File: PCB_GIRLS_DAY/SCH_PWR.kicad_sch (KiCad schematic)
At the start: 8 parts, among them J3 Conn_01x03_Pin, U3 AP2112K-3.3, U4 AMS1117-5.0

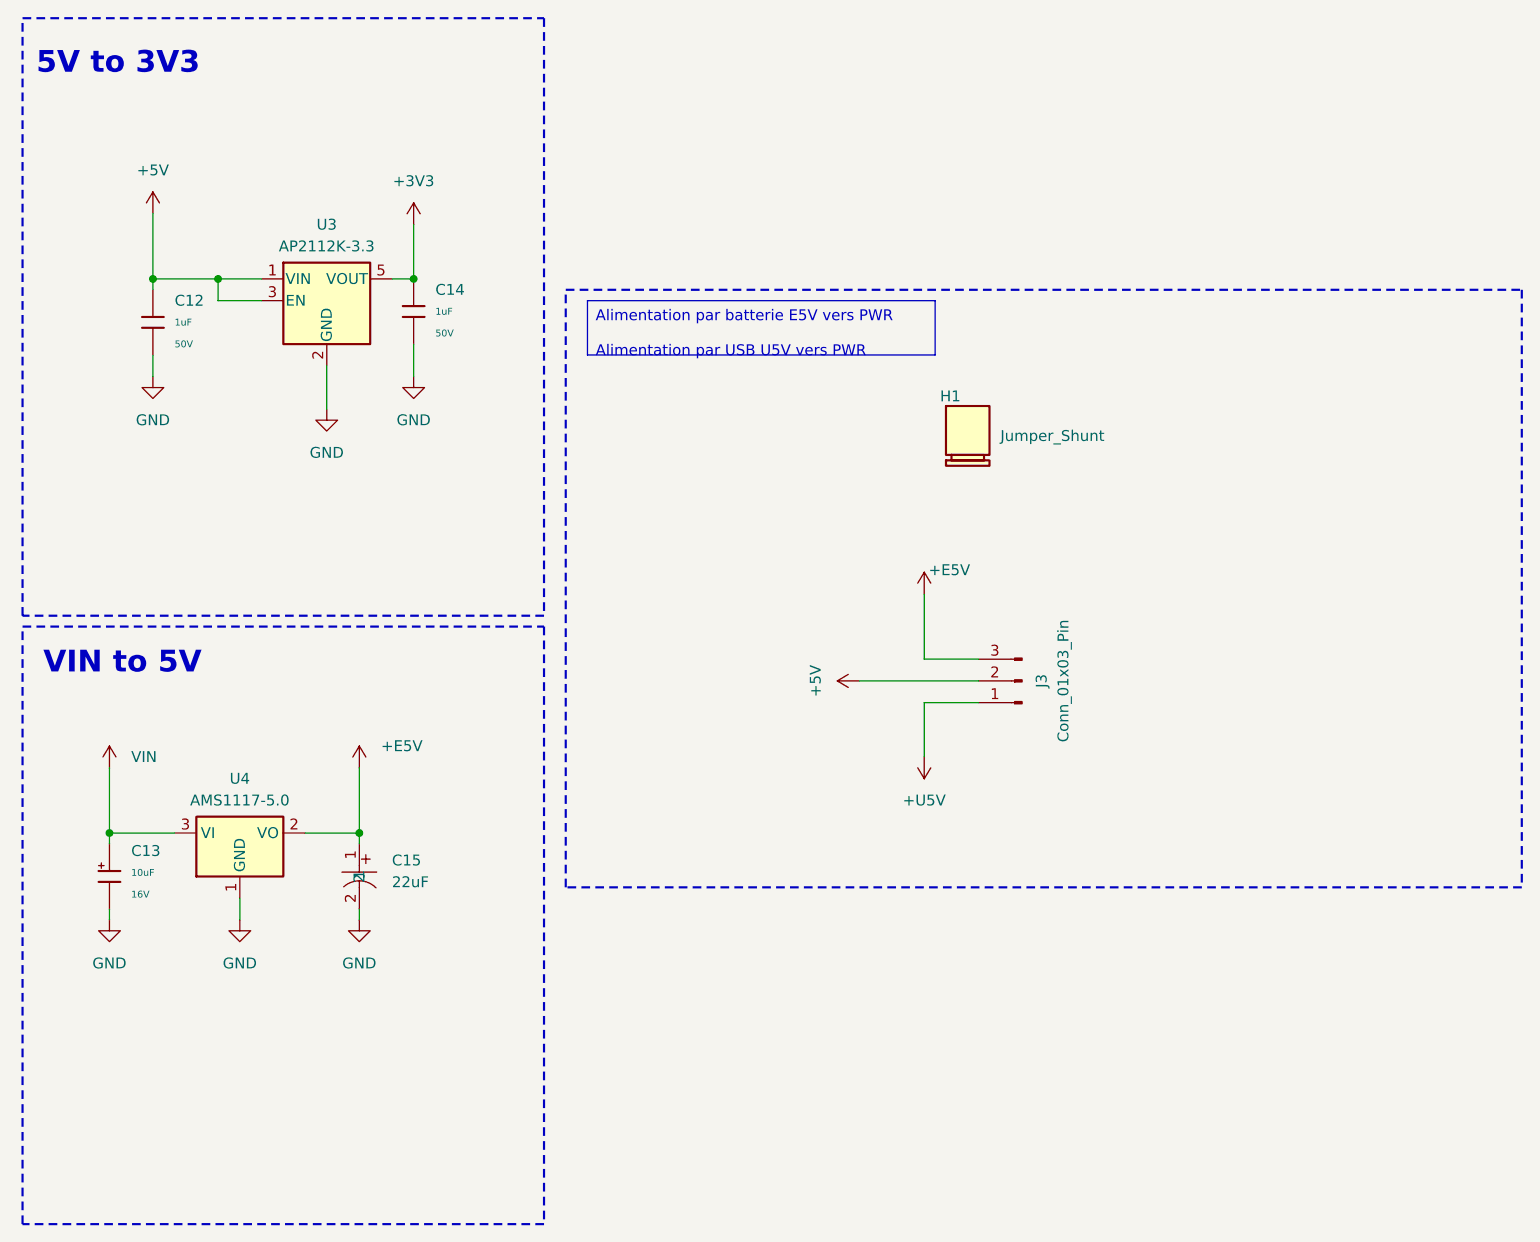
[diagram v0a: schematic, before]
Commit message: Kicad - PCB avant routage
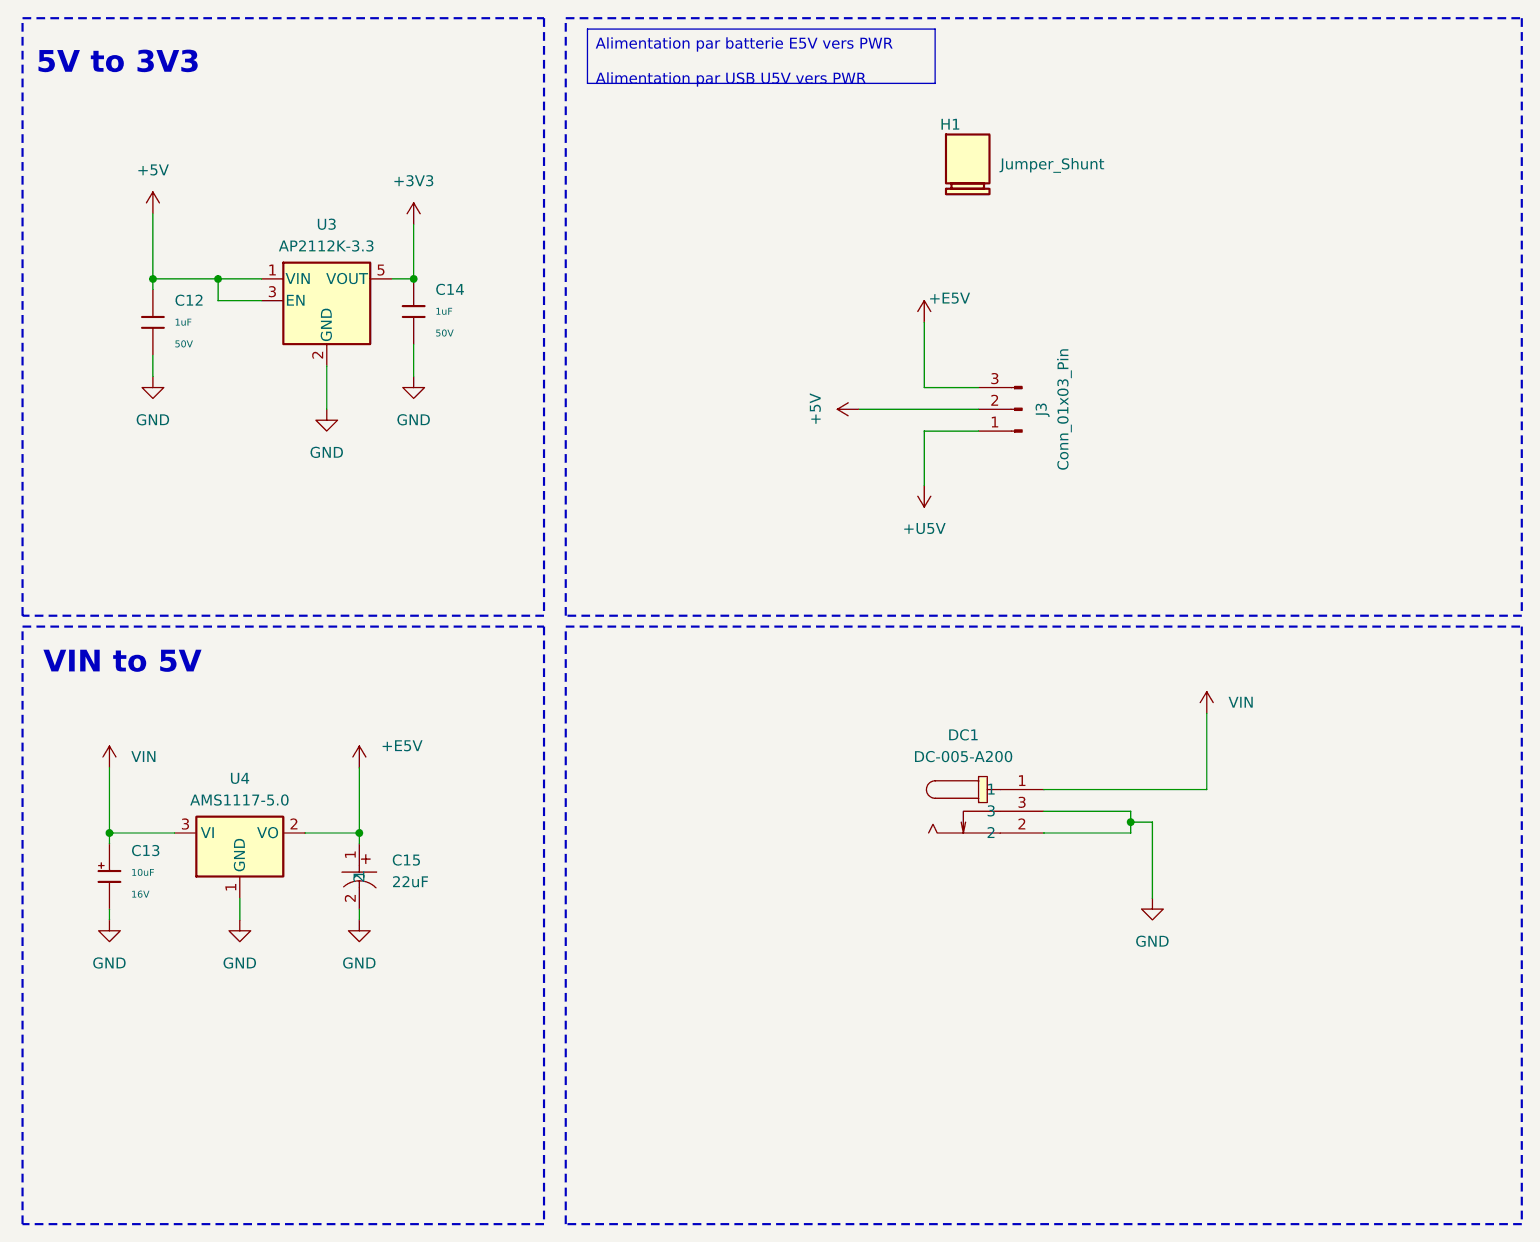
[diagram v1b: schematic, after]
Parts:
- added DC1: DC-005-A200, EasyEDA:DC-IN-TH_DC-005-A200, symbol EasyEDA:DC-005-A200
- C15: footprint EasyEDA:CAP-SMD_BD6.3-L6.6-W6.6-FD -> EasyEDA-CAP_22uF_Aluminium:CAP-SMD_BD6.3-L6.6-W6.6-FD
- J3: footprint (none) -> Connector_PinHeader_2.54mm:PinHeader_1x03_P2.54mm_Vertical
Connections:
- net GND: now also DC1.2, DC1.3
- net VIN: now also DC1.1
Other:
- moved on the sheet: H1, J3
